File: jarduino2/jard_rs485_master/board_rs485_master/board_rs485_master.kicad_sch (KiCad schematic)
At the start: 0 parts

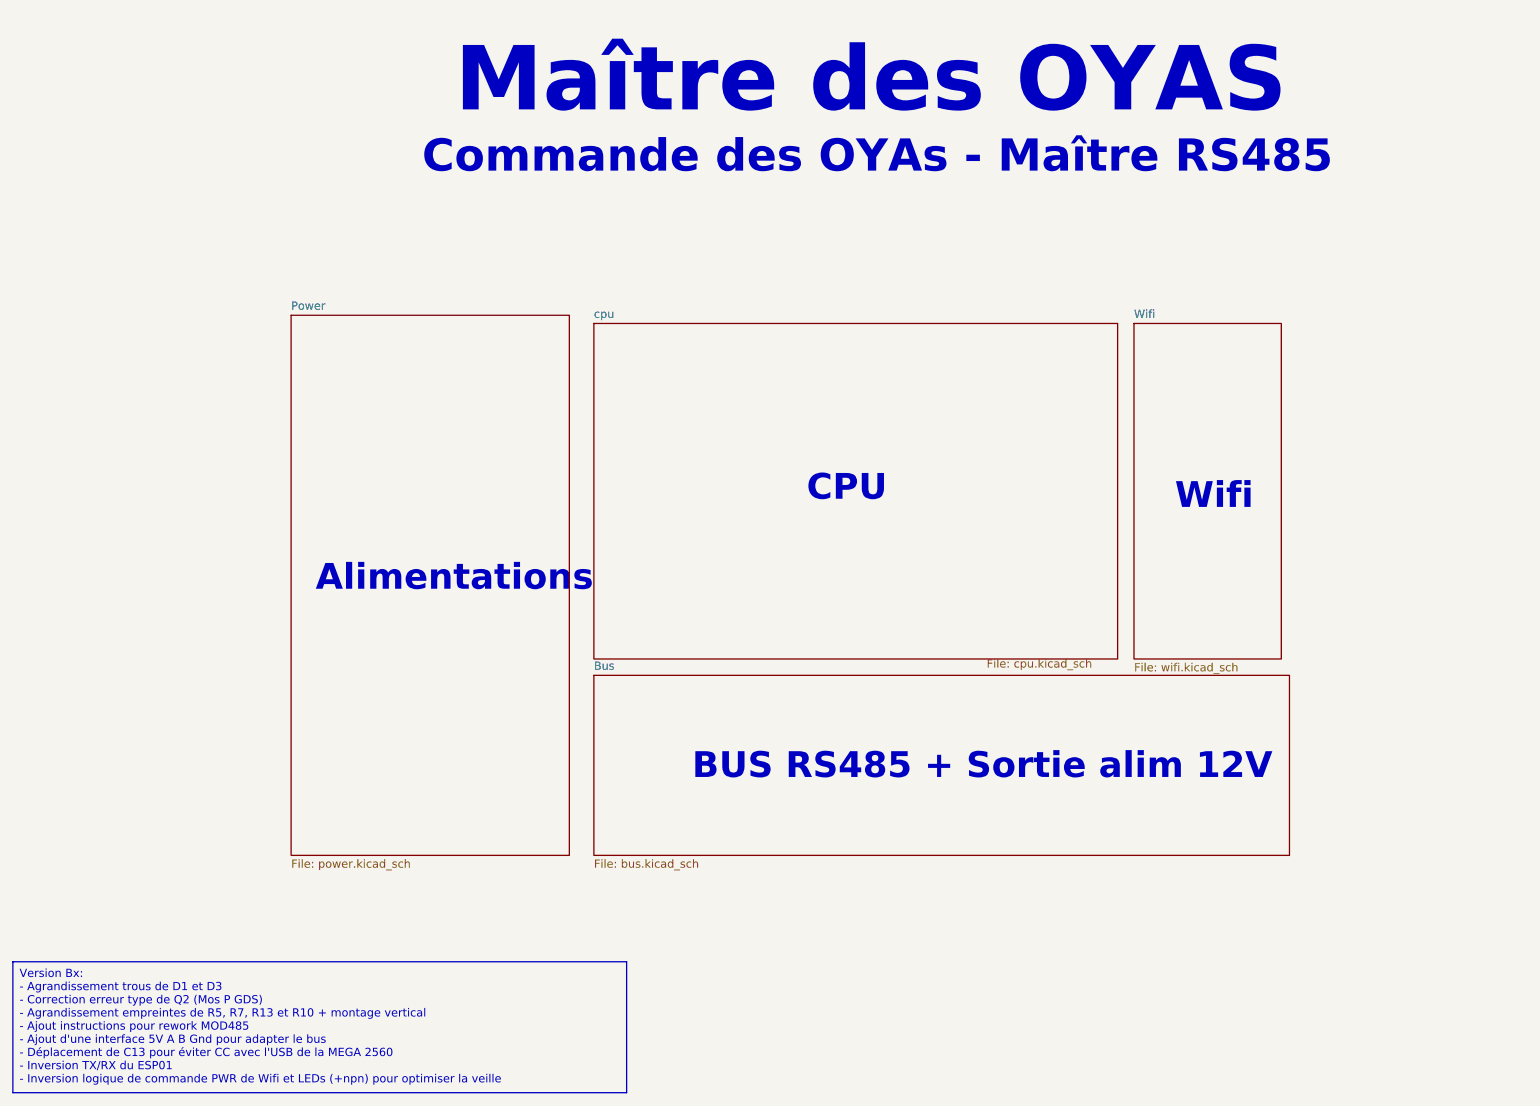
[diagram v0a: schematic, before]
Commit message: Réaffactation des commandes PWR de Wifi et LEDs (compatibilité soft) + suppression de la sheet Wifi sur le schéma (regreoupé dans UC)
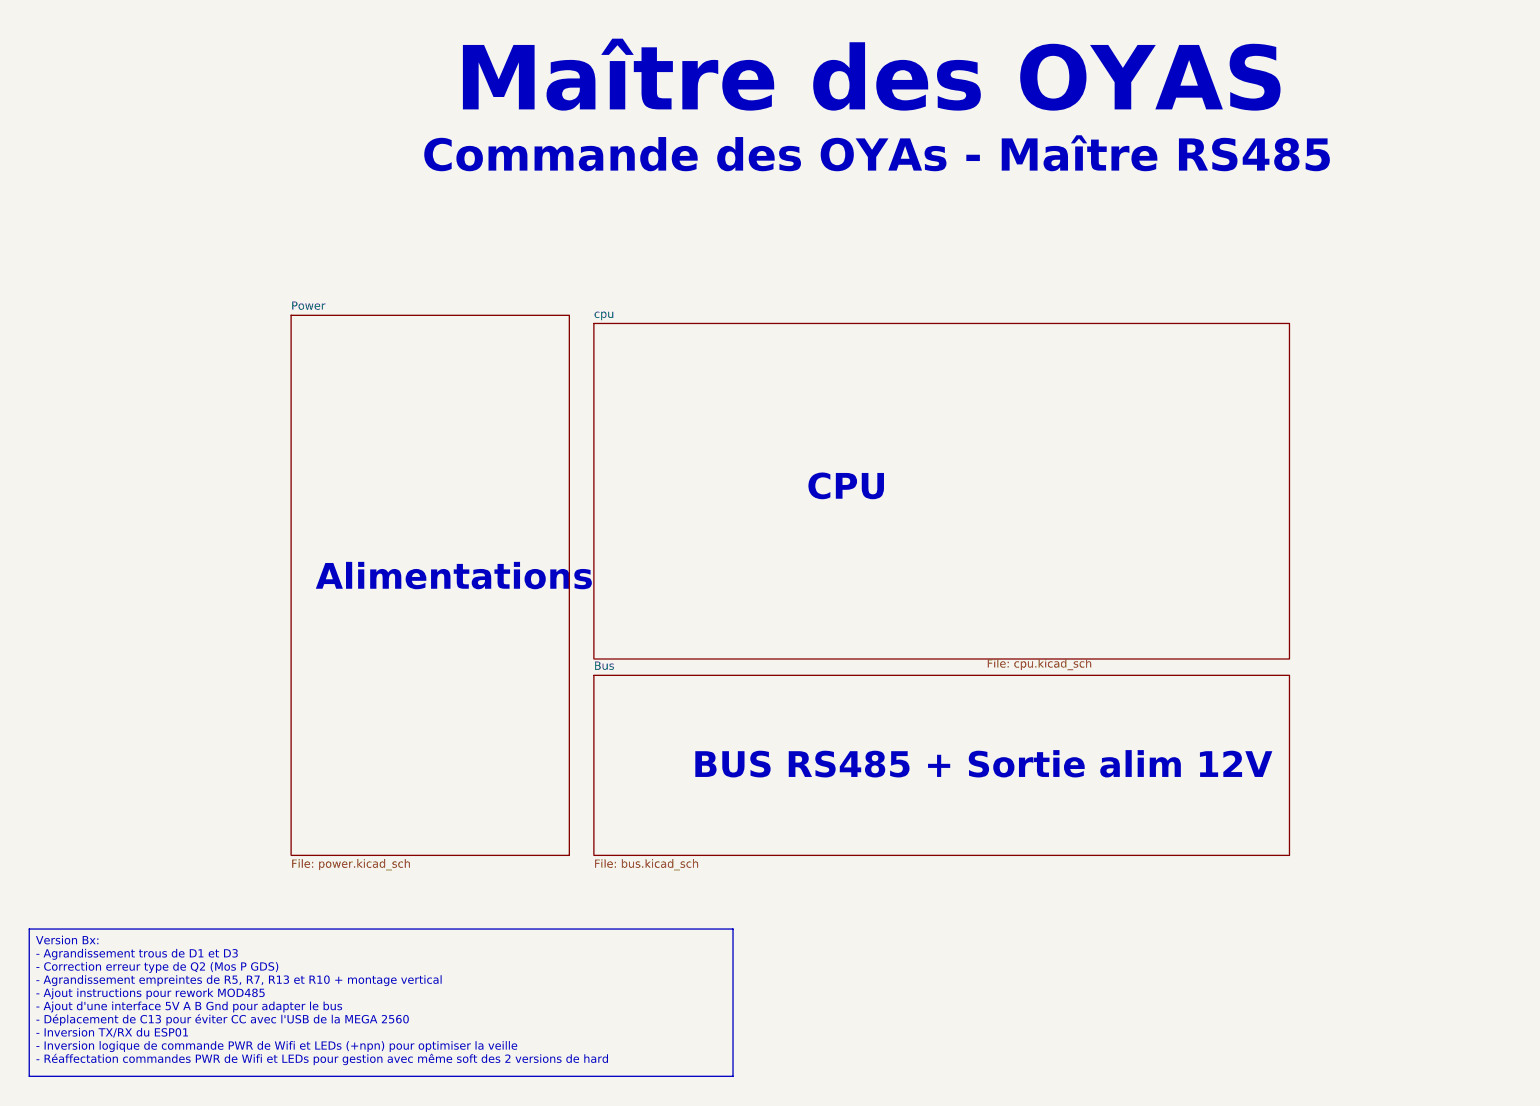
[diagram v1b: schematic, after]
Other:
- removed sheet Wifi
- note removed: "Wifi"
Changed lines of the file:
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@@
   (title_block
     (title "Commande des OYA - Maître RS485")
-    (date "2024-04-26")
+    (date "2024-05-06")
     (rev "B0")
     (company "BPC")
@@
     (comment 4 "Maître RS485 avec alim 12 V commutée")
   )
-  (text_box "Version Bx:\n  - Agrandissement trous de D1 et D3\n  - Correction erreur type de Q2 (Mos P GDS)\n  - Agrandissement empreintes de R5, R7, R13 et R10 + montage vertical\n  - Ajout instructions pour rework MOD485\n  - Ajout d'une interface 5V A B Gnd pour adapter le bus\n  - Déplacement de C13 pour éviter CC avec l'USB de la MEGA 2560\n  - Inversion TX/RX du ESP01\n  - Inversion logique de commande PWR de Wifi et LEDs (+npn) pour optimiser la veille\n"
-    (at 25.4 167.64 0) (size 95.25 20.32)
+  (text_box "Version Bx:\n  - Agrandissement trous de D1 et D3\n  - Correction erreur type de Q2 (Mos P GDS)\n  - Agrandissement empreintes de R5, R7, R13 et R10 + montage vertical\n  - Ajout instructions pour rework MOD485\n  - Ajout d'une interface 5V A B Gnd pour adapter le bus\n  - Déplacement de C13 pour éviter CC avec l'USB de la MEGA 2560\n  - Inversion TX/RX du ESP01\n  - Inversion logique de commande PWR de Wifi et LEDs (+npn) pour optimiser la veille\n  - Réaffectation commandes PWR de Wifi et LEDs pour gestion avec même soft des 2 versions de hard\n"
+    (at 27.94 162.56 0) (size 109.22 22.86)
     (stroke (width 0) (type default))
     (fill (type none))
@@
   )
   (text "BUS RS485 + Sortie alim 12V" (at 130.81 139.7 0)
-    (effects (font (face "Arial") (size 4 4) bold) (justify left bottom))
-  )
-  (text "Wifi" (at 205.74 97.79 0)
     (effects (font (face "Arial") (size 4 4) bold) (justify left bottom))
   )
@@
     )
   )
-  (sheet (at 199.39 68.58) (size 22.86 52.07) (fields_autoplaced)
-    (stroke (width 0.1524) (type solid))
-    (fill (color 0 0 0 0.0000))
-    (property "Sheetname" "Wifi" (at 199.39 67.8684 0)
-      (effects (font (size 1.27 1.27)) (justify left bottom))
-    )
-    (property "Sheetfile" "wifi.kicad_sch" (at 199.39 121.2346 0)
-      (effects (font (size 1.27 1.27)) (justify left top))
-    )
-    (property "Field2" "" (at 199.39 68.58 0)
-      (effects (font (size 1.27 1.27)) hide)
-    )
-    (instances
-      (project "board_rs485_master"
-        (path "/27904310-f1aa-47e2-a2a6-8db936442bd1" (page "5"))
-      )
-    )
-  )
   (sheet (at 115.57 123.19) (size 107.95 27.94) (fields_autoplaced)
     (stroke (width 0.1524) (type solid))
@@
     )
   )
-  (sheet (at 115.57 68.58) (size 81.28 52.07)
+  (sheet (at 115.57 68.58) (size 107.95 52.07)
     (stroke (width 0.1524) (type solid))
     (fill (color 0 0 0 0.0000))
